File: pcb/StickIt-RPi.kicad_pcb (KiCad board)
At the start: 2 copper layers, 65 x 56 mm, 39 parts, among them CON1 BARREL_JACK, J1 JSHORTNORMAL, J3 XuLA_IO_HDR, J4 JSHORTNORMAL, J5 JSHORTNORMAL, SW1 SW_PUSH, U1 NCV1117, U2 EEPROM_I2C

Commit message: Updated component reference identifiers.
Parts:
- renumbered J3 to J1, J1 to J3, JP3 to JP1, JP8 to JP10, JP4 to JP2, JP5 to JP3, JP9 to JP4, JP1 to JP5, JP2 to JP6, JP10 to JP7, JP6 to JP8, JP7 to JP9

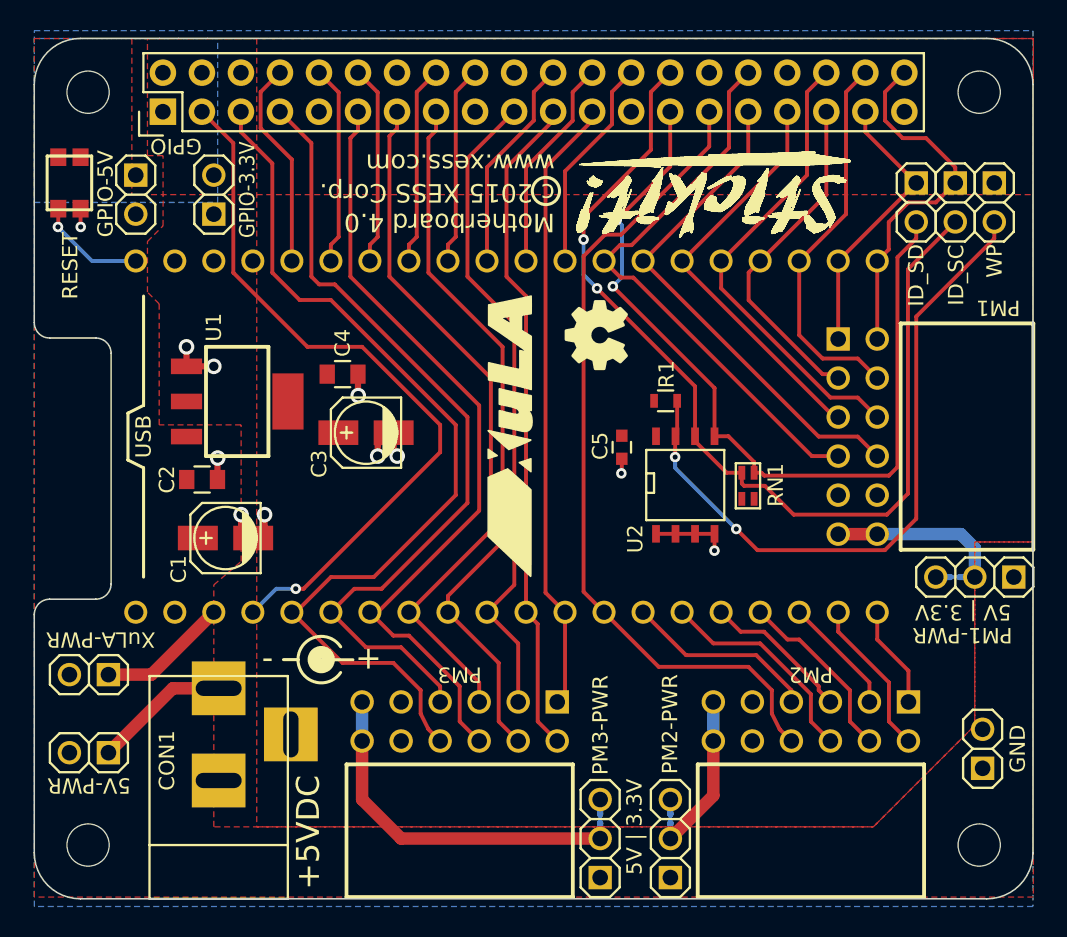
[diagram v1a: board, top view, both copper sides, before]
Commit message: Added Grove connectors.
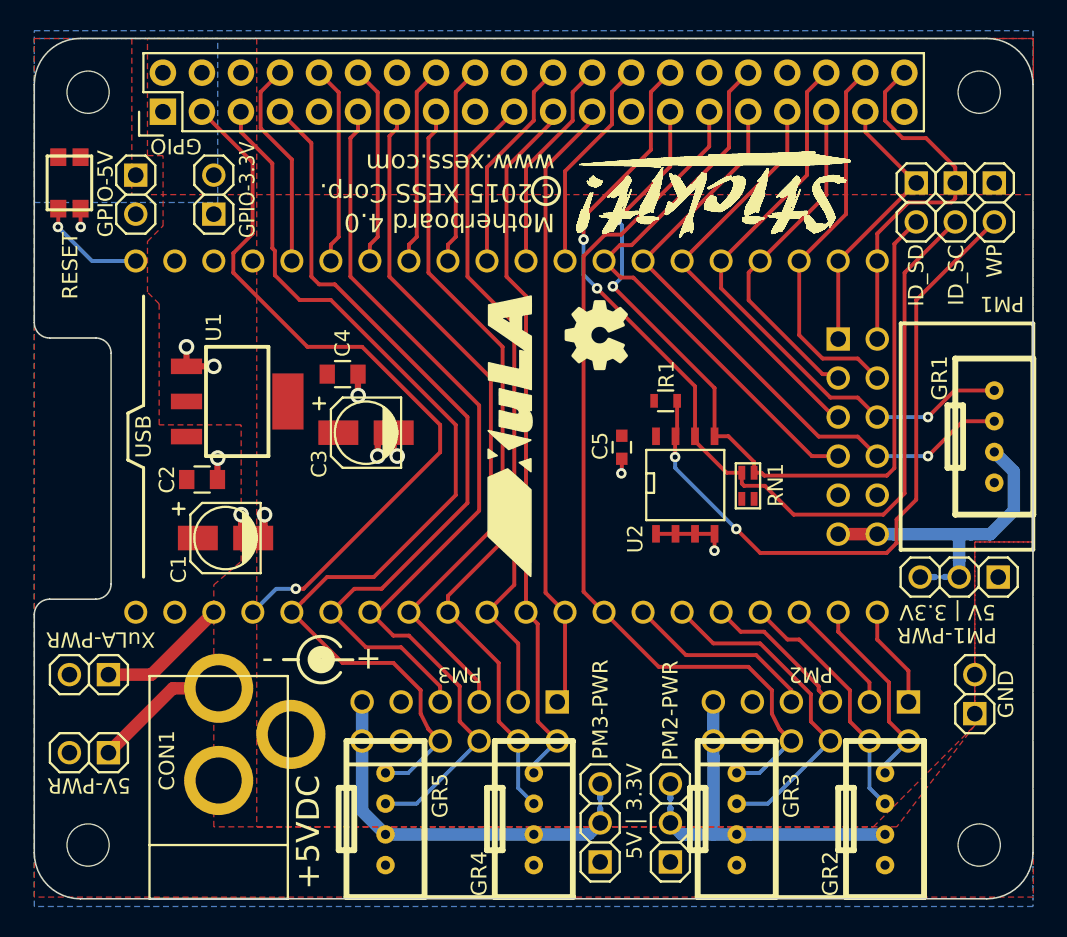
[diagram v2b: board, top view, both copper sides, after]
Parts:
- added GR1: Grove, XESS:GROVE_MALE, F.Cu at (62.5, 26.4)
- added GR2: Grove, XESS:GROVE_MALE, F.Cu at (55.4, 51.3)
- added GR3: Grove, XESS:GROVE_MALE, F.Cu at (45.7, 51.3)
- added GR4: Grove, XESS:GROVE_MALE, F.Cu at (32.5, 51.3)
- added GR5: Grove, XESS:GROVE_MALE, F.Cu at (22.9, 51.3)
- moved TP1 3.59 mm to (61.2, 43.2)
- moved J5 1.02 mm to (36.8, 50.6)
- moved JP2 1.02 mm to (41.4, 51.6)
- moved JP3 1.02 mm to (36.8, 51.6)
- moved J3 1.02 mm to (59.2, 35.5)
- moved J4 1.02 mm to (41.4, 50.6)
- moved JP1 1.02 mm to (60.2, 35.6)
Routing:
- net Net-(GR2-Pad3): track 11.1 -> 23.9 mm
- net CHAN5: track 33.1 -> 41.6 mm, vias 0 -> 1
- net CHAN3: track 30.5 -> 38.8 mm, vias 0 -> 1
- net Net-(GR1-Pad3): track 12.2 -> 20.2 mm
- net CHAN20: track 14.2 -> 22.0 mm
- net CHAN28: track 51.4 -> 59.2 mm
- net CHAN18: track 11.8 -> 16.3 mm
- net CHAN26: track 46.5 -> 51.0 mm
- net CHAN30: track 60.0 -> 64.4 mm
- net CHAN22: track 53.9 -> 58.3 mm
- net CHAN16: track 10.3 -> 13.0 mm
- net CHAN24: track 43.6 -> 46.3 mm
- net CHAN31: track 47.2 -> 48.2 mm
- net CHANCLK: track 23.8 -> 24.4 mm

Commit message: Changed PCB footprints for reset switch, capacitors and resistor.
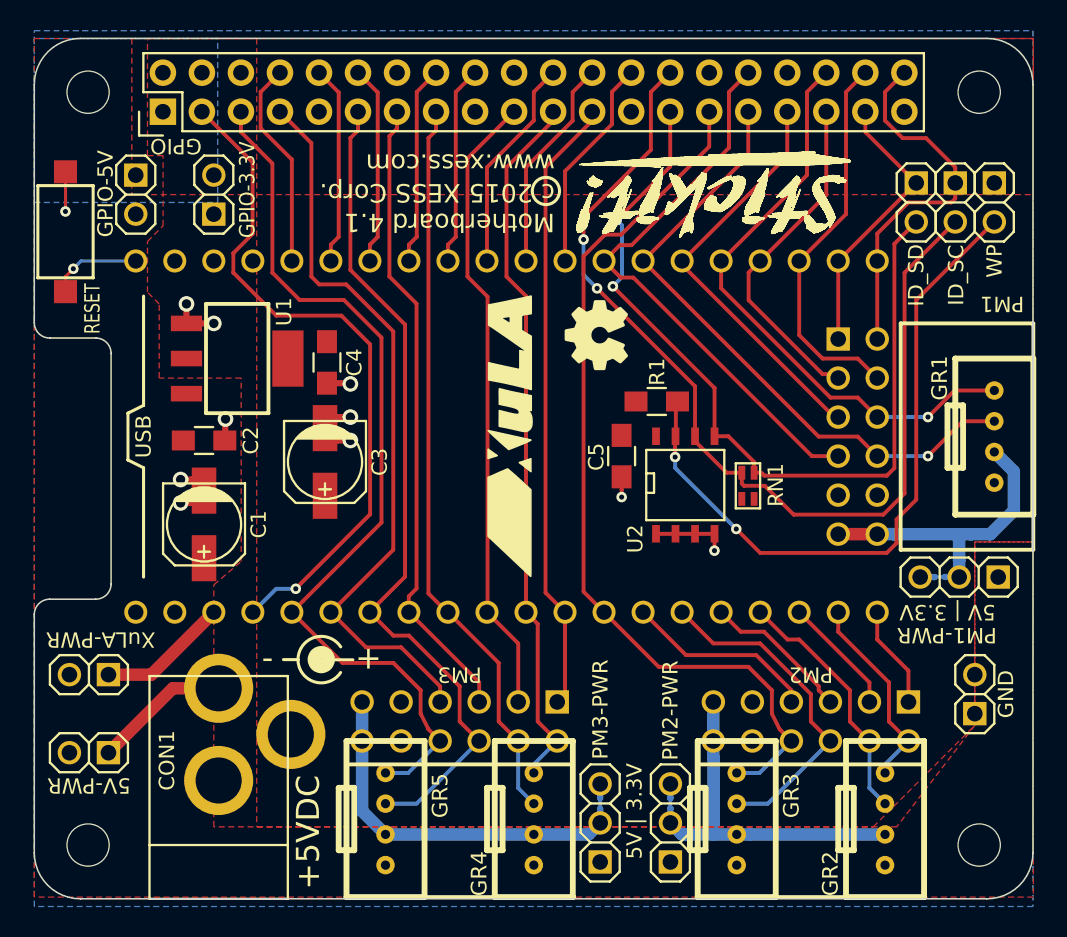
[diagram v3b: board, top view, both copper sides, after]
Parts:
- C1, C3: footprint Capacitors_SMD:c_elec_4x5.7 -> Capacitors_SMD:c_elec_5x5.3
- C2, C4: footprint Capacitors_SMD:C_0805 -> Resistors_SMD:R_0805_HandSoldering
- C5: footprint Capacitors_SMD:C_0603 -> Resistors_SMD:R_0805_HandSoldering
- R1: footprint Resistors_SMD:R_0603 -> Resistors_SMD:R_0805_HandSoldering
- SW1: footprint XESS:SW_EVP-AA002 -> XESS:RS-282G05A3-SM_RT
- U2: value EEPROM_I2C -> CAT24C32
- moved C3 3.28 mm to (18.9, 28.1), turned to 270 degrees
- moved SW1 3.19 mm to (2.03, 13.1)
- moved U1 2.79 mm to (13.2, 21.3)
- moved C2 2.54 mm to (11.0, 26.7)
- moved C1 1.66 mm to (11.0, 32.1), turned to 270 degrees
- moved C4 1.27 mm to (19.1, 21.6), turned to 270 degrees
- moved R1 0.58 mm to (40.5, 24.1)
- moved C5 0.58 mm to (38.2, 27.7)
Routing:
- net CHAN30: track 64.4 -> 59.1 mm
- net CHAN29: track 53.1 -> 48.5 mm
- net CHAN28: track 59.2 -> 54.9 mm
- net CHAN27: track 45.5 -> 41.5 mm
- net CHAN31: track 48.2 -> 44.5 mm
- net CHAN26: track 51.0 -> 48.1 mm
- net GND: track 20.4 -> 22.9 mm
- net CHAN25: track 42.5 -> 41.1 mm
- net Net-(J1-Pad40): track 7.18 -> 5.97 mm
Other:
- board text added: "Motherboard 4.1 c 2015 XESS Corp. www.xess.com"
- board text removed: "Motherboard 4.0 c 2015 XESS Corp. www.xess.com"

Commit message: Removed two Grove connectors and rotated the others.
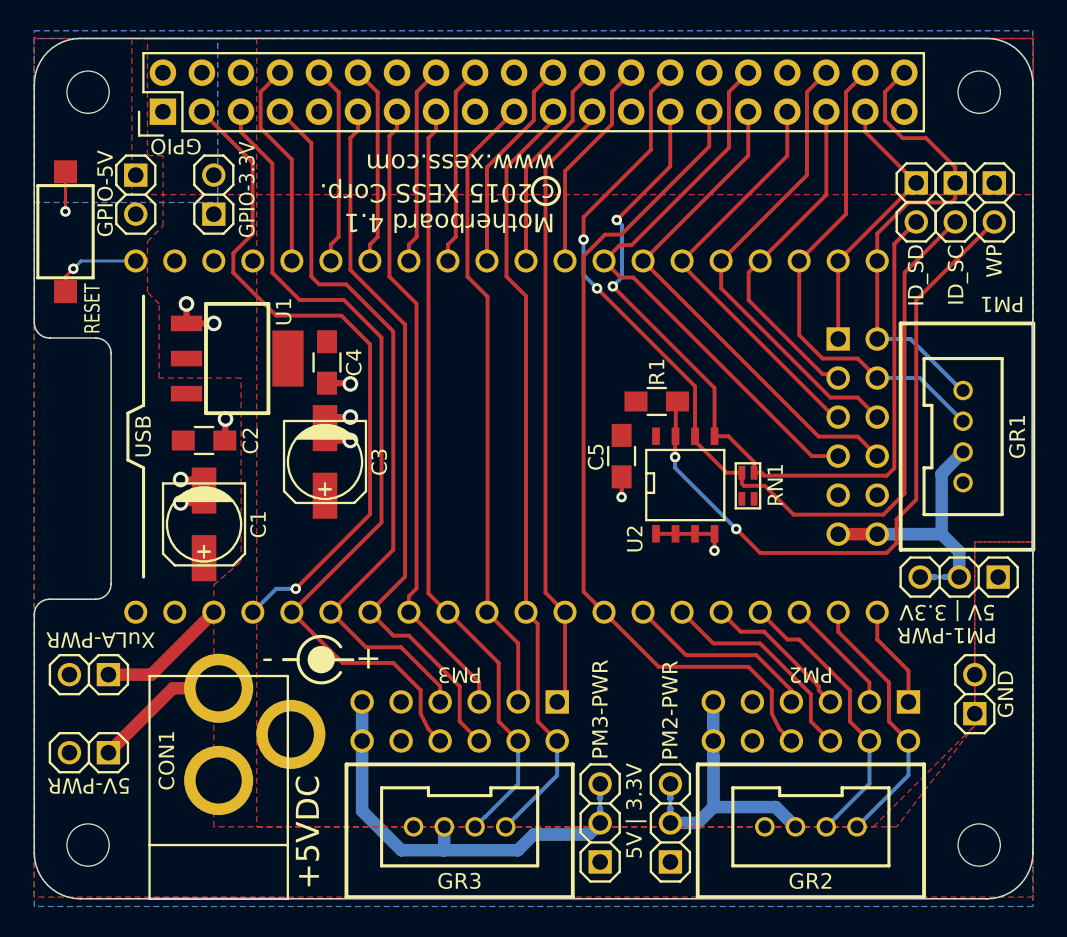
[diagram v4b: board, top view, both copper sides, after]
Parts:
- removed the ? at (30.7, 10.4)
- removed the ? at (36.6, 19.8)
- removed the ? at (53.1, 7.87)
- removed the ? at (20.0, 24.6)
- removed G***: LOGO, XESS Logos:LOGO-XULA-18x3
- removed GR4, GR5: Grove, XESS:GROVE_MALE
- added ?: , XESS:xesscorp2, B.Cu at (32.1, 26.3)
- added ?: , XESS Logos:oshw_logo_6mm, B.Cu at (31.1, 10.3)
- moved GR3 18.0 mm to (27.7, 51.8), turned to 180 degrees
- moved GR2 4.85 mm to (50.5, 51.8), turned to 180 degrees
- moved GR1 2.03 mm to (60.5, 26.4)
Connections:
- GR1 pad 1: CHAN3 -> CHANCLK
- GR1 pad 2: CHAN5 -> CHAN1
- GR3 pad 1: CHAN22 -> CHAN24
- GR3 pad 2: CHAN20 -> CHAN26
- GR3 pad 3: Net-(GR2-Pad3) -> Net-(GR3-Pad3)
- J5 pad 1: Net-(GR4-Pad3) -> Net-(GR3-Pad3)
- JP3 pad 2: Net-(GR4-Pad3) -> Net-(GR3-Pad3)
- PM3 pad 12: Net-(GR4-Pad3) -> Net-(GR3-Pad3)
- PM3 pad 6: Net-(GR4-Pad3) -> Net-(GR3-Pad3)
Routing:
- net Net-(GR3-Pad3): track 0.00 -> 26.9 mm
- net Net-(GR4-Pad3): track 24.5 -> 0.00 mm
- net CHAN5: track 41.6 -> 33.1 mm, vias 1 -> 0
- net CHAN3: track 38.8 -> 30.5 mm, vias 1 -> 0
- net CHAN28: track 54.9 -> 47.1 mm
- net CHAN20: track 22.0 -> 14.2 mm
- net CHANCLK: track 24.4 -> 31.4 mm
- net Net-(GR2-Pad3): track 23.9 -> 16.9 mm
- net CHAN1: track 25.1 -> 31.9 mm
- net CHAN22: track 58.3 -> 53.9 mm
- net CHAN30: track 59.1 -> 54.7 mm
- net CHAN24: track 46.3 -> 50.6 mm
- net CHAN16: track 13.0 -> 17.3 mm
- net Net-(GR1-Pad3): track 20.2 -> 16.9 mm
- net CHAN18: track 16.3 -> 18.5 mm
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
